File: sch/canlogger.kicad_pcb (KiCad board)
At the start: 4 copper layers, 50 x 40 mm, 98 parts, among them J1 DE9_Pins_MountingHoles, J2 2x7P Pitch:1.27mm, Q1 NTD2955T4G, Q2 IRLML0060, Q3 IRLML0060, SW1 TS-1087S-01526, U1 STM32G474CBT6, U2 TJA1051T/3, U3 TJA1051T/3, U4 CH340N, U5 AP63205WU-7, U6 LD1117S33CTR, X1 GT-TF003-H0185-02, Y1 16MHz

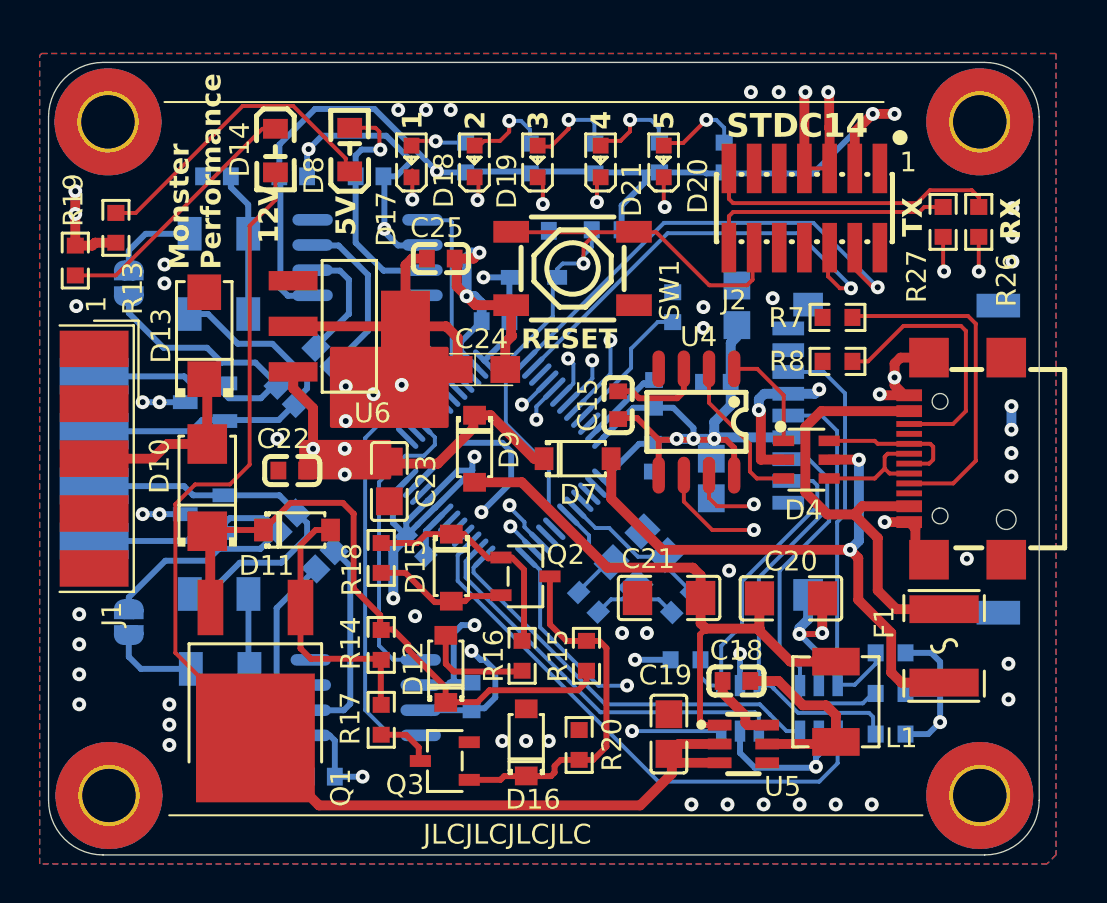
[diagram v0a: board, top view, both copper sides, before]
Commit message: Fix SPI pins add 3.3v led
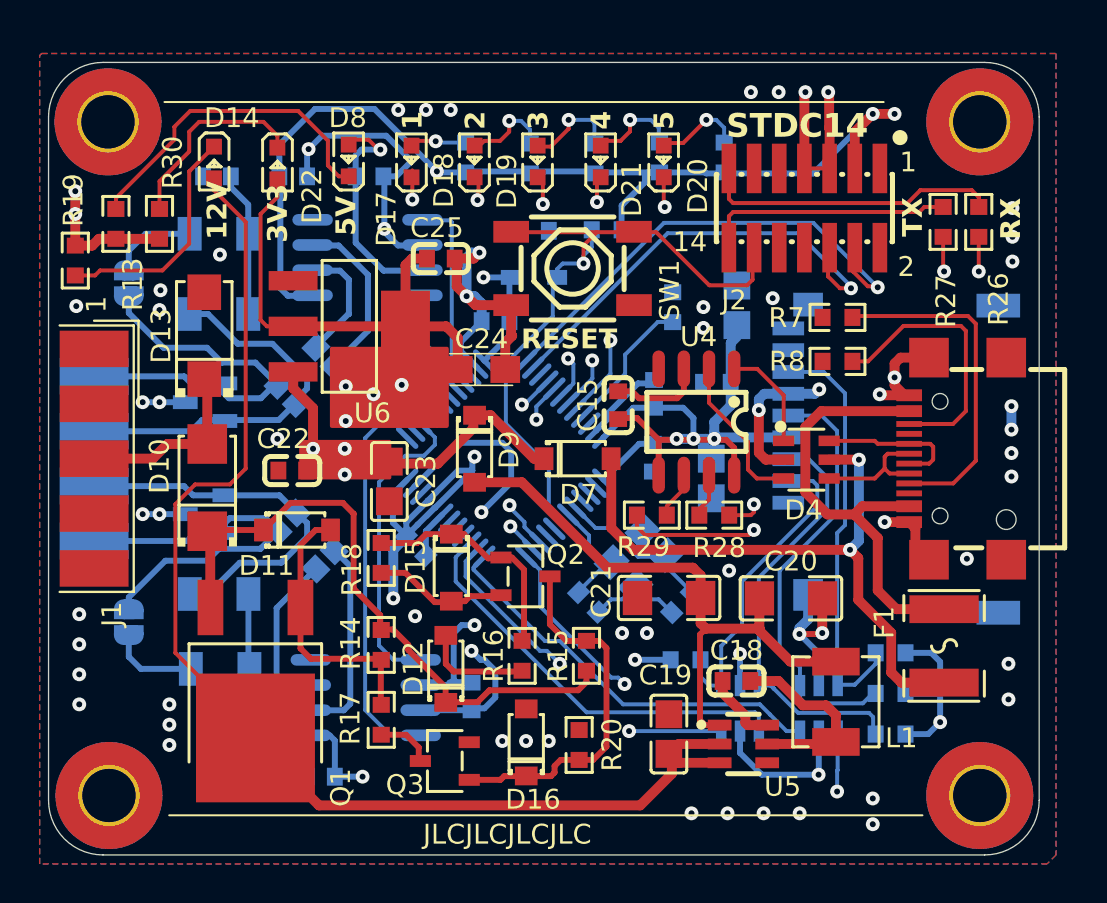
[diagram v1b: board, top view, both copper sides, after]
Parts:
- added D22: ~, EasyEDA_Lib:LED0603-RD, F.Cu at (116.5, 98.6)
- added R28: 0, EasyEDA_Lib:R0603, F.Cu at (138.6, 116.3)
- added R29: 0, EasyEDA_Lib:R0603, F.Cu at (135.4, 116.3)
- added R30: 330, EasyEDA_Lib:R0603, F.Cu at (110.6, 101.7)
- D14, D8: value LED -> ~; footprint EasyEDA_Lib:LED0805-RD_GREEN -> EasyEDA_Lib:LED0603-RD
- moved D14 3.16 mm to (113.3, 98.5)
- moved D8 0.55 mm to (120.2, 98.5)
- moved R13 0.20 mm to (108.4, 101.7)
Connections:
- U1 pad 14: SPI1_MOSI -> SPI1_MISO
- U1 pad 15: SPI1_MISO -> SPI1_MOSI
- U4 pad 6: UART_USB_RX -> Net-(U4-TXD)
- U4 pad 7: UART_USB_TX -> Net-(U4-RXD)
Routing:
- net +3V3: track 287.2 -> 297.8 mm
- net Net-(D22-K): track 0.00 -> 10.1 mm
- net Net-(U4-TXD): track 0.00 -> 2.37 mm
- net GND: track 116.8 -> 119.1 mm, vias 64 -> 65
- net Net-(U4-RXD): track 0.00 -> 2.22 mm
- net UART_USB_TX: track 36.2 -> 34.3 mm
- net Net-(D8-K): track 15.7 -> 17.0 mm
- net Net-(D14-K): track 13.2 -> 11.8 mm
- net UART_USB_RX: track 39.3 -> 40.6 mm
- net SPI1_MISO: track 27.6 -> 28.7 mm, vias 0 -> 2
- net SPI1_MOSI: track 20.1 -> 21.1 mm
- net VBUS: track 31.3 -> 32.2 mm
- net SD_CS: track 16.4 -> 15.8 mm
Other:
- board text added: "14"
- board text added: "3V3"
- board text added: "v1.0"

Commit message: change 2x22u to 3x10u plot all order jlcpcb + lcsc
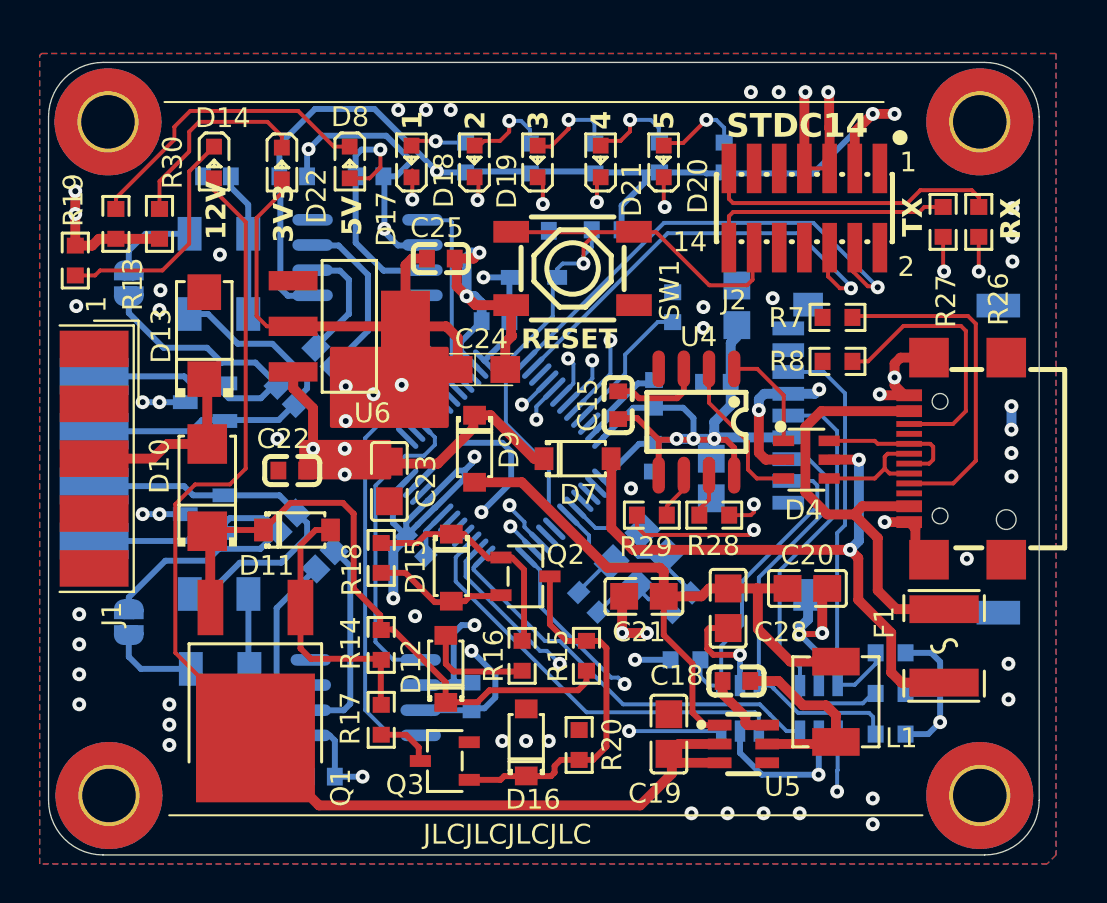
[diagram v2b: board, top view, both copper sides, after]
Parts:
- added C28: 10u, EasyEDA_Lib:C0805, F.Cu at (139.3, 121.0)
- C20, C21: value 22uF -> 10u; footprint canlogger_custom_lib:C1206 -> EasyEDA_Lib:C0805
- moved C21 1.27 mm to (135.1, 120.5)
- moved C20 0.97 mm to (143.3, 120.0)
- moved D22 0.23 mm to (116.8, 98.6)
- moved D8 0.11 mm to (120.2, 98.5), turned to -90 degrees
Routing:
- net GND: track 119.1 -> 127.2 mm
- net +5V_IN: track 31.0 -> 33.9 mm
- net Net-(D8-K): track 17.0 -> 15.7 mm
- net +5V: track 72.0 -> 72.6 mm
